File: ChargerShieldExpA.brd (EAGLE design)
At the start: 161.3 x 99.1 mm, 82 parts, among them IC1 LM324N, IC2 TL431, Q1 BD648, Q2 BUZ11, Q3 BUZ171, T2 BC548, X1 +5V, X2 Battery, X3 VCC

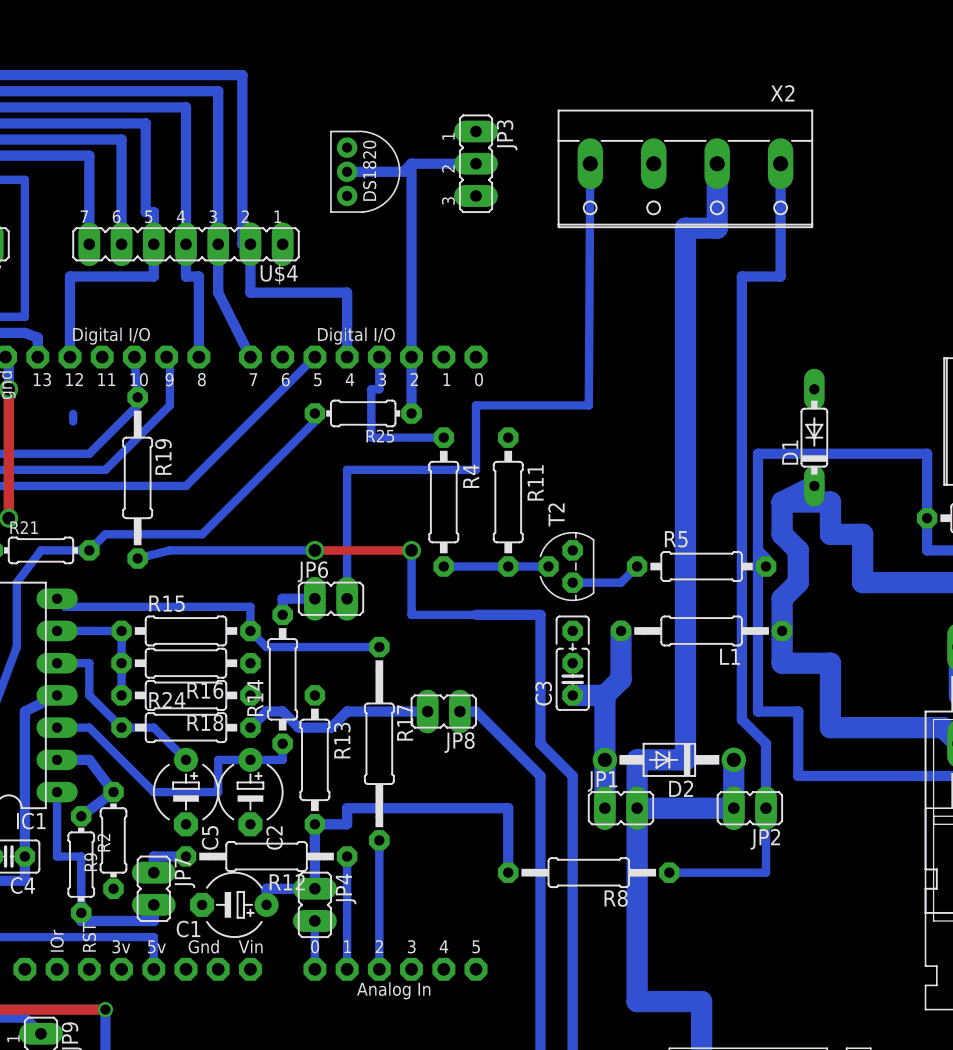
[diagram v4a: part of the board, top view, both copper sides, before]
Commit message: difference amplifier at charge current
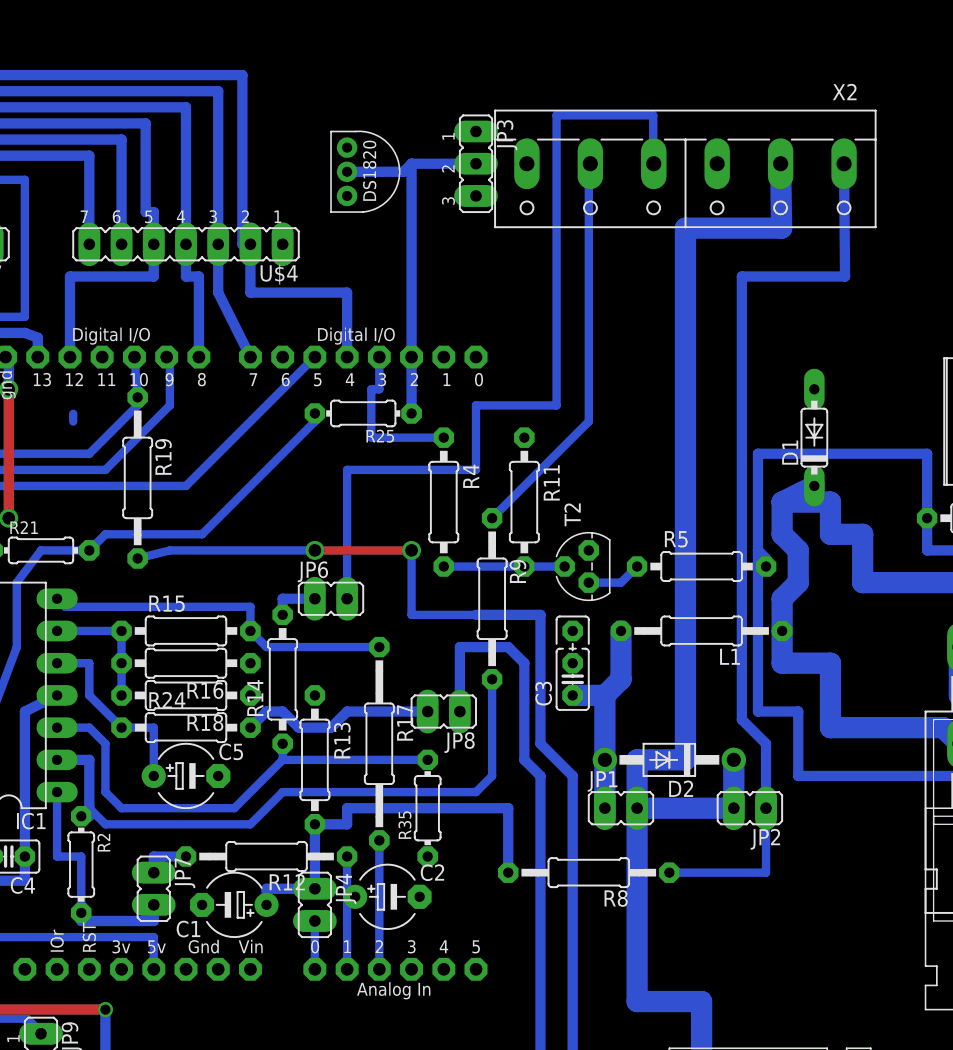
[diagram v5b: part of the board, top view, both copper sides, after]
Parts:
- added R35: 100k, rcl:0204/7
- R14: value 1k -> 10k
- R9: device rcl:0204/7 -> rcl:0207/12
- X2: device con-wago-500:W237-4 -> con-wago-500:W237-6
- moved R9 35.4 mm to (64.8, 31.8), turned to 270 degrees
- moved C2 13.6 mm to (56.5, 8.26), turned to 0 degrees
- moved C5 1.27 mm to (40.6, 17.8), turned to 0 degrees
- moved R11 1.27 mm to (67.3, 39.4)
- moved T2 1.27 mm to (72.4, 34.3)
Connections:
- net I_SENSE renamed I1_SENSE+
- new net I1_SENSE-: R9.1, X2.5
- net GND: now also R35.1, X2.6; no longer R9.1, X2.3
- net I_BATT1: now also C2.+
- net N$15: now also R35.2; no longer C2.+
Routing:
- net N$14: track 8.89 -> 49.1 mm
- net I1_SENSE-: track 0.00 -> 31.2 mm
- net N$15: track 23.7 -> 36.9 mm
- net I1_SENSE+: track 53.3 -> 66.1 mm
- net N$25: track 52.9 -> 64.6 mm
- net N$8: track 67.5 -> 72.6 mm
- net N$13: track 105.4 -> 110.5 mm
- net N$6: track 5.61 -> 4.34 mm
- net N$5: track 8.26 -> 9.52 mm
- net I_BATT1: track 8.89 -> 9.79 mm

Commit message: arrangement
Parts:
- added JP15: (no value), bigger:JP1
- moved C2 0.90 mm to (57.1, 7.62)
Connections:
- new net N$35: JP15.2, R17.1
- net N$17: now also JP15.1; no longer R17.1
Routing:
- net N$17: track 28.1 -> 23.0 mm
- net N$35: track 0.00 -> 2.54 mm
- net I_DISC1: track 10.2 -> 12.7 mm
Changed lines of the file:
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@@
 <setting verticaltext="up"/>
 </settings>
-<grid distance="0.05" unitdist="inch" unit="mm" style="lines" multiple="1" display="yes" altdistance="0.025" altunitdist="inch" altunit="mm"/>
+<grid distance="2.54" unitdist="mm" unit="mm" style="lines" multiple="1" display="yes" altdistance="1.27" altunitdist="mm" altunit="mm"/>
 <layers>
 <layer number="1" name="Top" color="4" fill="1" visible="yes" active="yes"/>
@@
 <element name="C1" library="rcl" package="E5-5" value="10µ" x="44.45" y="7.62" rot="R180"/>
 <element name="R14" library="rcl" package="0207/10" value="10k" x="48.26" y="25.4" rot="R90"/>
-<element name="C2" library="rcl" package="E5-5" value="3µ3" x="56.515" y="8.255"/>
+<element name="C2" library="rcl" package="E5-5" value="3µ3" x="57.15" y="7.62"/>
 <element name="R15" library="rcl" package="0207/10" value="100k" x="40.64" y="29.21"/>
 <element name="R16" library="rcl" package="0207/10" value="33k" x="40.64" y="26.67" rot="R180"/>
@@
 <element name="R34" library="rcl" package="0204/7" value="0" x="10.16" y="33.02" rot="R180"/>
 <element name="R35" library="rcl" package="0204/7" value="100k" x="59.69" y="15.24" rot="R90"/>
+<element name="JP15" library="bigger" package="JP1" value="" x="52.07" y="27.94" rot="R270"/>
 </elements>
 <signals>
@@
 <contactref element="R12" pad="1"/>
 <contactref element="U$1" pad="A1"/>
-<wire x1="53.34" y1="2.54" x2="53.34" y2="8.89" width="0.6604" layer="16"/>
+<wire x1="53.34" y1="2.54" x2="53.34" y2="7.62" width="0.6604" layer="16"/>
 <contactref element="C2" pad="+"/>
-<wire x1="53.34" y1="8.89" x2="53.34" y2="11.43" width="0.6604" layer="16"/>
-<wire x1="53.34" y1="8.89" x2="53.975" y2="8.255" width="0.6604" layer="16"/>
+<wire x1="53.34" y1="7.62" x2="53.34" y2="11.43" width="0.6604" layer="16"/>
+<wire x1="54.61" y1="7.62" x2="53.34" y2="7.62" width="0.8128" layer="16"/>
 </signal>
 <signal name="N$16">
@@
 <contactref element="IC1" pad="7"/>
 <contactref element="R15" pad="2"/>
-<contactref element="R17" pad="1"/>
 <wire x1="46.99" y1="27.94" x2="45.72" y2="29.21" width="0.6604" layer="16"/>
-<wire x1="55.88" y1="27.94" x2="46.99" y2="27.94" width="0.6604" layer="16"/>
 <wire x1="45.72" y1="31.115" x2="31.115" y2="31.115" width="0.6604" layer="16"/>
 <wire x1="31.115" y1="31.115" x2="30.48" y2="31.75" width="0.6604" layer="16"/>
 <wire x1="45.72" y1="29.21" x2="45.72" y2="31.115" width="0.6604" layer="16"/>
+<contactref element="JP15" pad="1"/>
+<wire x1="50.8" y1="27.94" x2="46.99" y2="27.94" width="0.8128" layer="16"/>
 </signal>
 <signal name="I_DISC1">
+<contactref element="U$1" pad="A2"/>
 <contactref element="R17" pad="2"/>
-<contactref element="U$1" pad="A2"/>
-<wire x1="55.88" y1="2.54" x2="55.88" y2="12.7" width="0.6604" layer="16"/>
+<wire x1="55.88" y1="12.7" x2="55.88" y2="10.16" width="0.8128" layer="16"/>
+<wire x1="55.88" y1="10.16" x2="57.15" y2="10.16" width="0.8128" layer="16"/>
+<wire x1="57.15" y1="10.16" x2="57.15" y2="5.08" width="0.8128" layer="16"/>
+<wire x1="57.15" y1="5.08" x2="55.88" y2="5.08" width="0.8128" layer="16"/>
+<wire x1="55.88" y1="5.08" x2="55.88" y2="2.54" width="0.8128" layer="16"/>
 </signal>
 <signal name="N$20">
@@
 <wire x1="72.39" y1="66.04" x2="72.51" y2="66.04" width="0.6604" layer="16"/>
 </signal>
+<signal name="N$35">
+<contactref element="R17" pad="1"/>
+<contactref element="JP15" pad="2"/>
+<wire x1="53.34" y1="27.94" x2="55.88" y2="27.94" width="0.8128" layer="16"/>
+</signal>
 </signals>

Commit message: power pins, Vin
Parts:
- added JP16, JP17, JP18: (no value), bigger:JP2
- R4: device rcl:0207/10 -> rcl:0207/15
- X1: value +5V -> +Vin
- moved X3 20.3 mm to (104.1, 66.0)
- moved R4 20.1 mm to (67.3, 58.4), turned to 0 degrees
- moved T2 16.9 mm to (76.2, 50.8)
- moved R11 16.7 mm to (69.8, 55.9), turned to 0 degrees
- moved R5 11.4 mm to (81.3, 45.7)
- moved R6 10.2 mm to (104.1, 48.3)
- moved R7 5.08 mm to (53.3, -11.4)
- moved U$2 1.42 mm to (53.3, 68.6)
- moved JP3 1.27 mm to (62.2, 66.0)
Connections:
- removed net VIN: U$1.VIN
- new net N$50: JP17.1, JP17.2, JP17.3, U$1.VIN, X1.1
- net +5V: now also JP16.1, JP16.2, JP16.3; no longer X1.1
- net GND: now also JP18.1, JP18.2, JP18.3
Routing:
- net N$50: track 0.00 -> 68.6 mm, vias 0 -> 2
- net GND: track 80.7 -> 59.1 mm
- net VCC: track 193.5 -> 213.8 mm
- net N$7: track 86.6 -> 97.8 mm
- net N$12: track 30.1 -> 37.5 mm
- net +5V: track 127.5 -> 120.6 mm
- net N$25: track 64.6 -> 69.6 mm
- net N$39: track 76.5 -> 73.9 mm
- net N$5: track 9.52 -> 7.66 mm
- net N$21: track 6.13 -> 7.62 mm
- net N$6: track 4.34 -> 3.81 mm

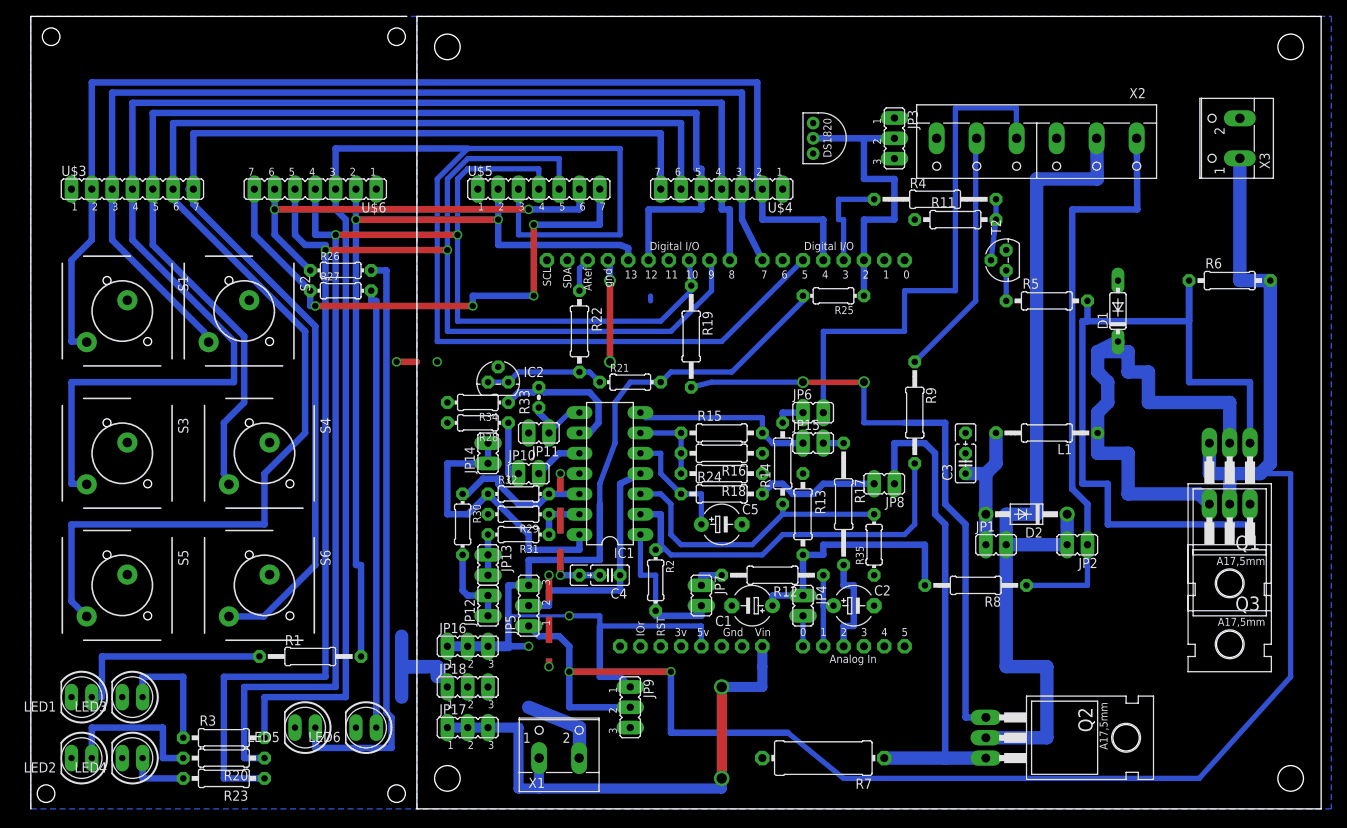
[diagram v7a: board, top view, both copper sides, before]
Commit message: boost converter
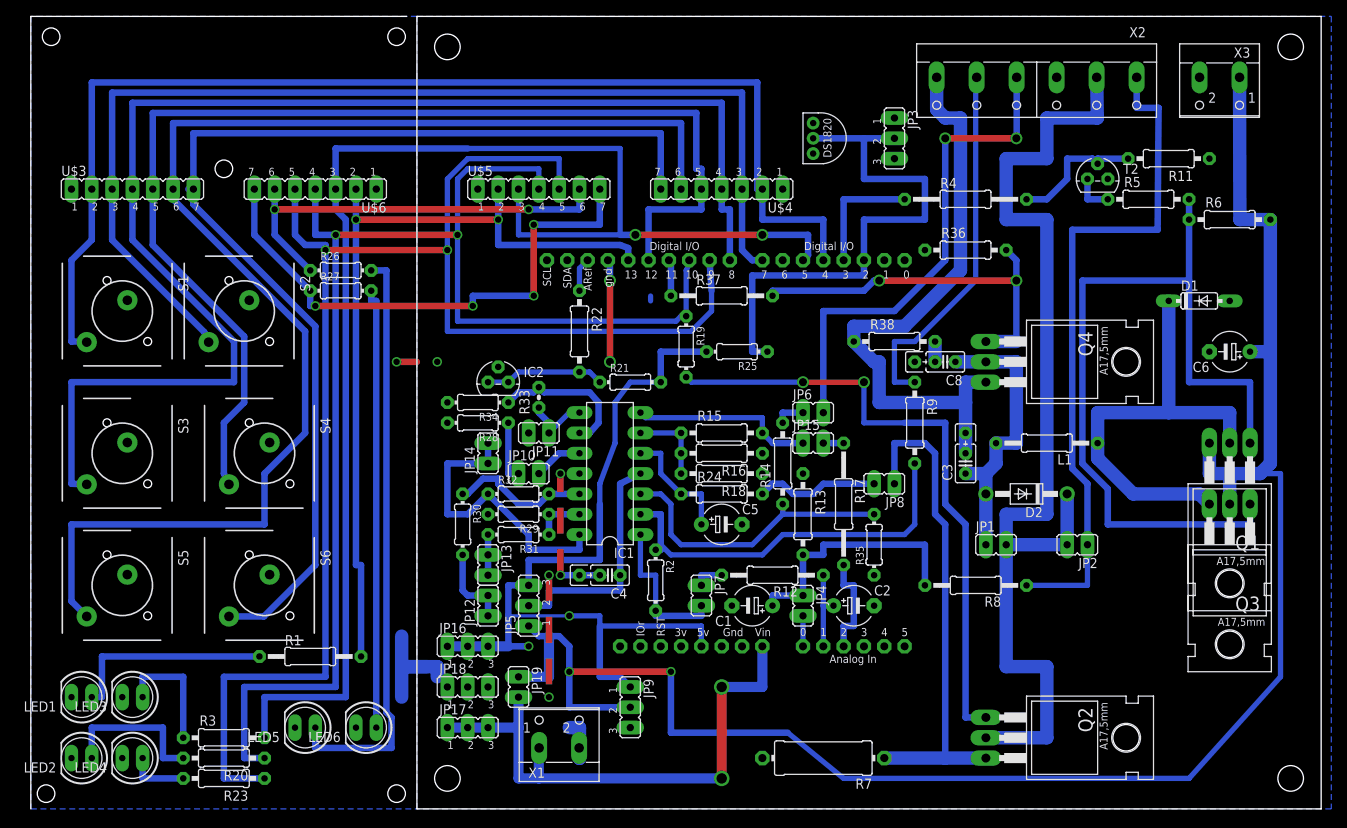
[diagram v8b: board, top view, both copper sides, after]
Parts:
- added C6: 10µ, rcl:E5-5
- added C8: 100n, rcl:C025_050-025X075
- added JP19: (no value), bigger:JP1
- added Q4: IRFZ48Z, transistor-power:TO220BH
- added R36: 1M, rcl:0207/10
- added R37: 200, rcl:0207/12
- added R38: 1k, rcl:0207/10
- R19: device rcl:0207/12 -> rcl:0204/7
- R9: device rcl:0207/12 -> rcl:0207/10
- moved R11 27.7 mm to (96.5, 63.5), turned to 180 degrees
- moved R5 18.0 mm to (94.0, 58.4)
- moved T2 15.3 mm to (87.6, 61.0), turned to 0 degrees
- moved R25 13.9 mm to (42.5, 39.4)
- moved D1 10.2 mm to (100.3, 45.7), turned to 0 degrees
- moved R6 7.62 mm to (104.1, 55.9)
- moved X2 7.62 mm to (80.0, 72.4)
- moved X3 6.48 mm to (102.9, 72.4), turned to 180 degrees
- moved R4 3.81 mm to (71.1, 58.4)
- moved D2 2.54 mm to (78.7, 21.6)
- moved R19 1.42 mm to (36.2, 40.0)
- moved L1 1.27 mm to (81.3, 27.9)
- moved R9 1.27 mm to (64.8, 30.5)
- moved X1 1.27 mm to (20.3, -8.89)
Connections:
- new net N$51: Q4.G, R36.2, R37.2
- new net VIN: JP17.1, JP17.2, JP17.3, JP19.2, U$1.VIN, X1.1
- net GND: now also C6.-, Q4.S, R36.1, R38.1
- net N$10: now also C8.1, Q4.D
- net N$50: now also C8.2, R38.2; no longer JP17.1, JP17.2, JP17.3, U$1.VIN, X1.1
- net PWM_CHARGE2: now also R37.1
- net VCC: now also C6.+, JP19.1
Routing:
- net GND: track 59.1 -> 134.7 mm
- net VIN: track 0.00 -> 69.9 mm, vias 0 -> 2
- net N$50: track 68.6 -> 2.54 mm, vias 2 -> 0
- net N$19: track 224.8 -> 176.0 mm, vias 0 -> 2
- net N$51: track 0.00 -> 47.4 mm, vias 0 -> 2
- net N$12: track 37.5 -> 67.9 mm
- net N$13: track 110.5 -> 130.8 mm
- net N$10: track 17.0 -> 36.1 mm
- net VCC: track 213.8 -> 232.8 mm
- net I1_SENSE-: track 31.2 -> 46.5 mm
- net +5V: track 120.6 -> 107.6 mm
- net N$8: track 72.6 -> 85.5 mm
- net N$5: track 7.66 -> 17.2 mm
- net N$9: track 65.4 -> 57.6 mm
- net N$7: track 97.8 -> 103.6 mm
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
